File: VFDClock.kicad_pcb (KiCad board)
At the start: 2 copper layers, 76.2 x 53.3 mm, 22 parts, among them J1 Barrel_Jack_MountingPin, P1 Power, P2 Analog, P3 Digital, P4 Digital, Q1 VFD_LD8035E, Q2 VFD_LD8035E, Q3 VFD_LD8035E, Q4 VFD_LD8035E, Q5 VFD_LD8035E, Q6 VFD_LD8035E, U1 IC_HT16K33, U2 RTC_DS3231

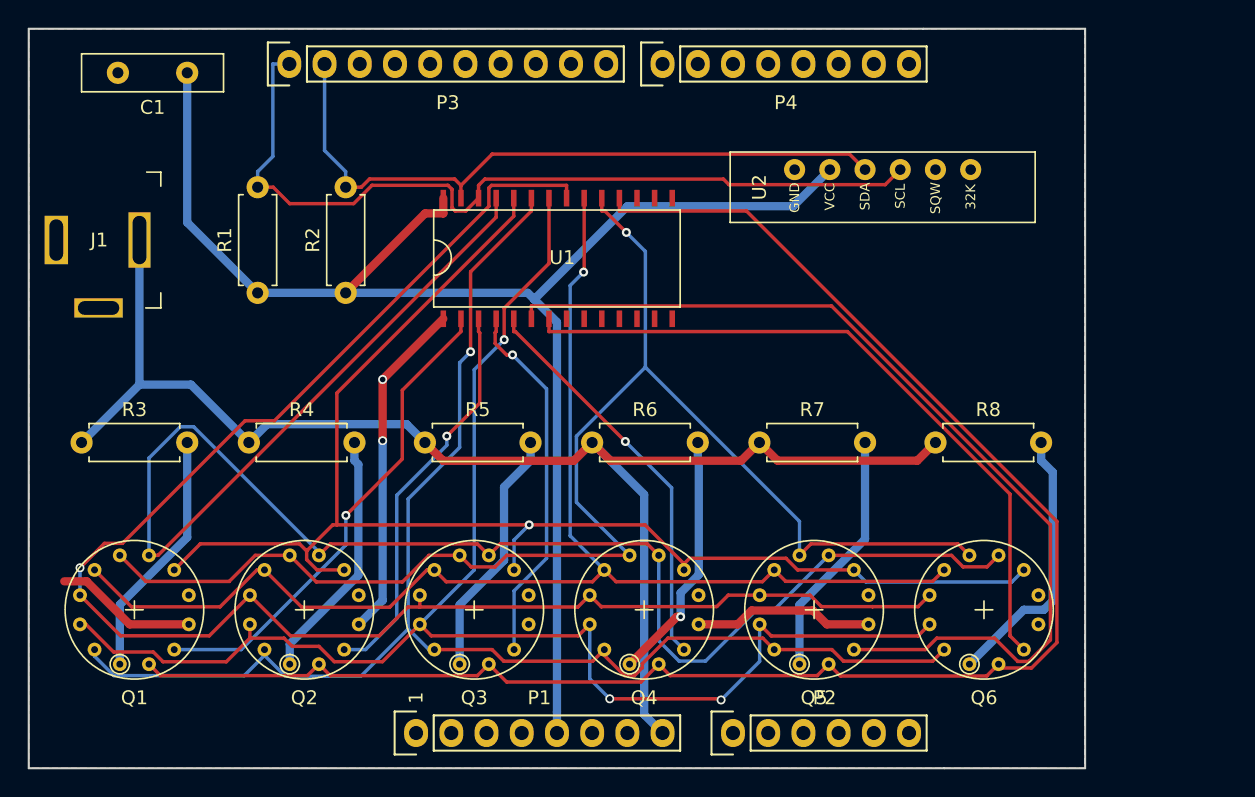
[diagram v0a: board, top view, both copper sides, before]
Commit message: 部品を仮配置
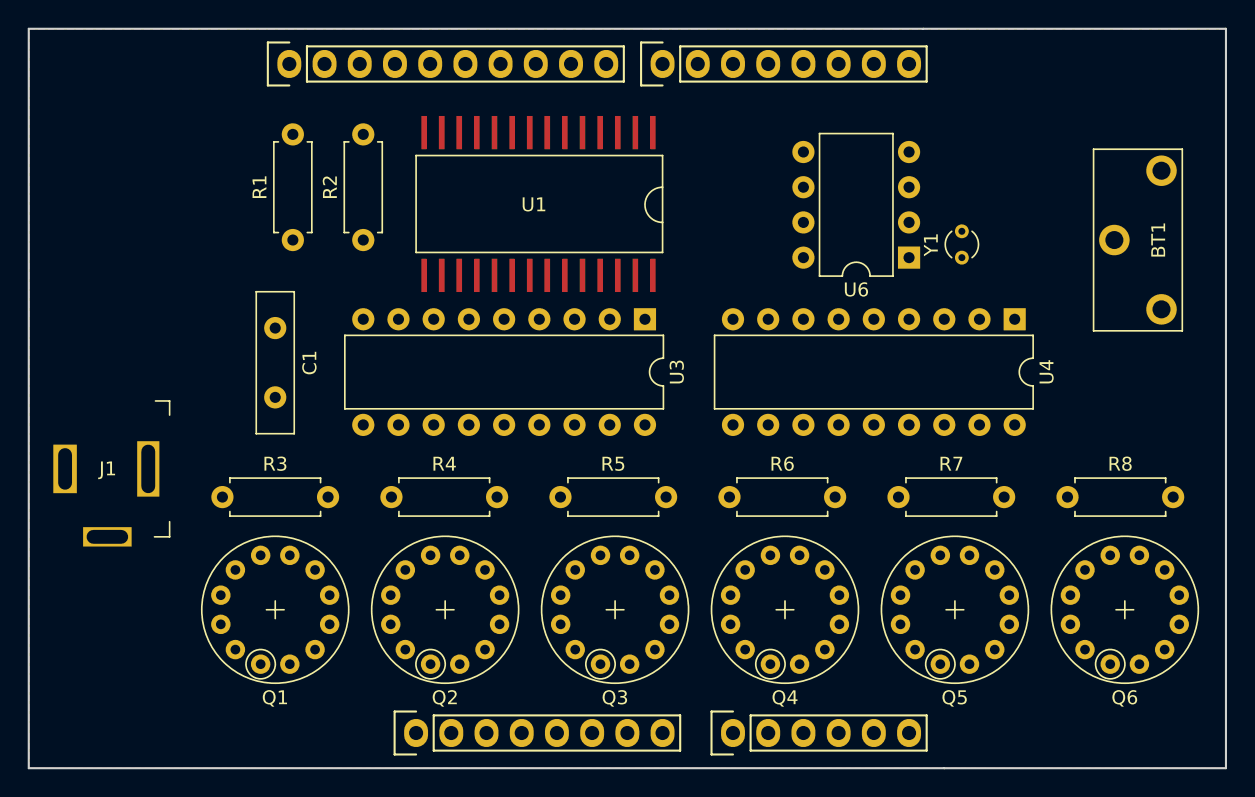
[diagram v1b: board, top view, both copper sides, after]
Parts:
- removed U2: RTC_DS3231, #MyFootPrints:RTC_DS3231_Vertical
- added BT1: Battery_Cell, #MyFootPrints:Battery_CR2032_CH74-2032LF, F.Cu at (191.0, 88.3)
- added U3: TBD62783APG, Package_DIP:DIP-18_W7.62mm, F.Cu at (155.4, 94.0)
- added U4: TBD62783APG, Package_DIP:DIP-18_W7.62mm, F.Cu at (182.1, 94.0)
- added U6: DS1307+, Package_DIP:DIP-8_W7.62mm, F.Cu at (174.5, 89.5)
- added Y1: 32.768kHz, Crystal:Crystal_DS26_D2.0mm_L6.0mm_Vertical, F.Cu at (178.3, 89.5)
- R3, R4, R5, R6, R7, R8: value 560 -> 510
- moved U1 20.1 mm to (156.7, 81.9), turned to 270 degrees
- moved C1 19.5 mm to (128.8, 94.6), turned to 270 degrees
- moved J1 16.5 mm to (105.9, 104.8)
- moved R4 11.0 mm to (137.2, 106.8)
- moved R3 10.9 mm to (125.0, 106.8)
- moved R7 10.8 mm to (173.7, 106.8)
- moved R6 10.7 mm to (161.5, 106.8)
- moved R5 10.5 mm to (149.4, 106.8)
- moved R8 10.3 mm to (185.9, 106.8)
- moved Q5 10.2 mm to (177.8, 114.9)
- moved Q1 10.2 mm to (128.8, 114.9)
- moved Q2 10.2 mm to (141.0, 114.9)
- moved Q3 10.2 mm to (153.3, 114.9)
- moved Q4 10.2 mm to (165.5, 114.9)
- moved Q6 10.2 mm to (190.1, 114.9)
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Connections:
- U1 pad 18: /dp -> Net-(U1-Pad18)
- U1 pad 19: /g -> Net-(U1-Pad19)
- U1 pad 2: Net-(Q1-Pad3) -> Net-(U1-Pad2)
- U1 pad 20: /f -> Net-(U1-Pad20)
- U1 pad 21: /e -> Net-(U1-Pad21)
- U1 pad 22: /d -> Net-(U1-Pad22)
- U1 pad 23: /c -> Net-(U1-Pad23)
- U1 pad 24: /b -> Net-(U1-Pad24)
- U1 pad 25: /a -> Net-(U1-Pad25)
- U1 pad 3: Net-(Q2-Pad3) -> Net-(U1-Pad3)
- U1 pad 4: Net-(Q3-Pad3) -> Net-(U1-Pad4)
- U1 pad 5: Net-(Q4-Pad3) -> Net-(U1-Pad5)
- U1 pad 6: Net-(Q5-Pad3) -> Net-(U1-Pad6)
- U1 pad 7: Net-(Q6-Pad3) -> Net-(U1-Pad7)
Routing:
- net /a: track 121.7 -> 0.00 mm
- net /dp: track 120.7 -> 0.00 mm
- net /e: track 118.6 -> 0.00 mm, vias 1 -> 0
- net /d: track 110.3 -> 0.00 mm, vias 3 -> 0
- net +5V: track 105.8 -> 0.00 mm
- net /c: track 104.7 -> 0.00 mm, vias 1 -> 0
- net +12V: track 102.9 -> 0.00 mm
- net /g: track 102.6 -> 0.00 mm, vias 1 -> 0
- net /b: track 102.1 -> 0.00 mm, vias 1 -> 0
- net /f: track 96.1 -> 0.00 mm, vias 1 -> 0
- net Net-(Q5-Pad3): track 69.1 -> 0.00 mm
- net /A5(SCL): track 61.6 -> 0.00 mm
- net Net-(Q6-Pad3): track 50.7 -> 0.00 mm
- net /A4(SDA): track 49.7 -> 0.00 mm
- net GND: track 47.9 -> 0.00 mm, vias 2 -> 0
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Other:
- board size 76.2 x 53.3 mm -> 86.4 x 53.3 mm
- board text removed: "1"

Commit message: 自動配線
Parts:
- moved U1 0.64 mm to (156.7, 81.3)
- turned BT1 to 270 degrees
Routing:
- net +12V: track 0.00 -> 150.4 mm
- net GND: track 0.00 -> 142.4 mm, vias 0 -> 1
- net /e: track 0.00 -> 112.1 mm, vias 0 -> 2
- net /dp: track 0.00 -> 107.5 mm, vias 0 -> 3
- net +5V: track 0.00 -> 101.0 mm, vias 0 -> 1
- net /b: track 0.00 -> 98.0 mm, vias 0 -> 1
- net /c: track 0.00 -> 96.2 mm
- net Net-(Q1-Pad3): track 0.00 -> 93.4 mm, vias 0 -> 1
- net /f: track 0.00 -> 92.2 mm, vias 0 -> 1
- net /a: track 0.00 -> 91.1 mm, vias 0 -> 2
- net /g: track 0.00 -> 88.7 mm
- net /d: track 0.00 -> 83.6 mm, vias 0 -> 1
- net /A5(SCL): track 0.00 -> 71.9 mm
- net /A4(SDA): track 0.00 -> 54.4 mm
- net Net-(Q2-Pad1): track 0.00 -> 47.1 mm, vias 0 -> 1
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
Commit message: ベタ修正
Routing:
- net GND: track 142.4 -> 108.1 mm
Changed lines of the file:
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@@
     (thickness 1.6)
     (drawings 14)
-    (tracks 569)
+    (tracks 565)
     (zones 0)
     (modules 26)
@@
     (trace_clearance 0.2)
     (zone_clearance 0.508)
-    (zone_45_only no)
+    (zone_45_only yes)
     (trace_min 0.2)
     (via_size 0.65)
@@
   (segment (start 186.395 120.65) (end 186.563 120.65) (width 0.6) (layer B.Cu) (net 2))
   (segment (start 181.732 115.987) (end 186.395 120.65) (width 0.6) (layer B.Cu) (net 2))
-  (segment (start 128.778 99.615) (end 118.778 99.615) (width 0.6) (layer B.Cu) (net 2))
-  (segment (start 118.778 99.615) (end 113.618 104.775) (width 0.6) (layer B.Cu) (net 2))
   (segment (start 135.128 101.6) (end 130.763 101.6) (width 0.6) (layer B.Cu) (net 2))
   (segment (start 130.763 101.6) (end 128.778 99.615) (width 0.6) (layer B.Cu) (net 2))
@@
   (segment (start 137.367 120.65) (end 148.463 120.65) (width 0.6) (layer B.Cu) (net 2))
   (segment (start 148.463 120.65) (end 151.638 123.825) (width 0.6) (layer B.Cu) (net 2))
-  (segment (start 156.023 79.88) (end 161.798 79.88) (width 0.6) (layer F.Cu) (net 2))
-  (segment (start 161.798 79.88) (end 161.798 79.88) (width 0.6) (layer F.Cu) (net 2))
-  (via (at 161.798 79.88) (size 0.65) (drill 0.4) (layers F.Cu B.Cu) (net 2))
   (segment (start 174.498 81.207876) (end 174.498 81.915) (width 0.6) (layer B.Cu) (net 2))
-  (segment (start 173.170124 79.88) (end 174.498 81.207876) (width 0.6) (layer B.Cu) (net 2))
-  (segment (start 161.798 79.88) (end 173.170124 79.88) (width 0.6) (layer B.Cu) (net 2))
+  (segment (start 156.023 79.88) (end 157.988 79.88) (width 0.6) (layer F.Cu) (net 2))
+  (segment (start 157.988 79.88) (end 157.988 79.88) (width 0.6) (layer F.Cu) (net 2))
+  (via (at 157.988 79.88) (size 0.65) (drill 0.4) (layers F.Cu B.Cu) (net 2))
   (segment (start 147.6584 81.4186) (end 147.6584 78.7605) (width 0.25) (layer F.Cu) (net 3))
   (segment (start 147.6584 78.7605) (end 148.0643 78.3546) (width 0.25) (layer F.Cu) (net 3))
@@
       )
     )
+  )
+  (zone (net 0) (net_name "") (layers F&B.Cu) (hatch edge 0.508)
+    (connect_pads (clearance 0.508))
+    (min_thickness 0.254)
+    (keepout (tracks allowed) (vias allowed) (copperpour not_allowed))
+    (fill (arc_segments 32) (thermal_gap 0.508) (thermal_bridge_width 0.508))
+    (polygon
+      (pts
+        (xy 195.453 117.475) (xy 192.278 120.65) (xy 126.238 120.65) (xy 124.333 118.745) (xy 124.333 112.395)
+        (xy 126.873 109.855) (xy 195.453 109.855)
+      )
+    )
+  )
+  (zone (net 0) (net_name "") (layer F.Cu) (hatch edge 0.508)
+    (connect_pads (clearance 0.508))
+    (min_thickness 0.254)
+    (keepout (tracks allowed) (vias allowed) (copperpour not_allowed))
+    (fill (arc_segments 32) (thermal_gap 0.508) (thermal_bridge_width 0.508))
+    (polygon
+      (pts
+        (xy 166.243 82.55) (xy 166.243 90.805) (xy 165.608 90.805) (xy 156.083 81.28) (xy 156.083 78.74)
+        (xy 162.433 78.74)
+      )
+    )
+  )
+  (zone (net 0) (net_name "") (layer F.Cu) (hatch edge 0.508)
+    (connect_pads (clearance 0.508))
+    (min_thickness 0.254)
+    (keepout (tracks allowed) (vias allowed) (copperpour not_allowed))
+    (fill (arc_segments 32) (thermal_gap 0.508) (thermal_bridge_width 0.508))
+    (polygon
+      (pts
+        (xy 161.798 106.045) (xy 160.528 106.045) (xy 160.528 102.235) (xy 164.338 102.235)
+      )
+    )
+  )
+  (zone (net 0) (net_name "") (layer F.Cu) (hatch edge 0.508)
+    (connect_pads (clearance 0.508))
+    (min_thickness 0.254)
+    (keepout (tracks allowed) (vias allowed) (copperpour not_allowed))
+    (fill (arc_segments 32) (thermal_gap 0.508) (thermal_bridge_width 0.508))
+    (polygon
+      (pts
+        (xy 161.163 92.71) (xy 161.163 94.615) (xy 159.258 96.52) (xy 159.258 104.775) (xy 156.083 104.775)
+        (xy 154.813 106.045) (xy 150.368 106.045) (xy 147.828 107.315) (xy 131.318 107.315) (xy 131.318 99.695)
+        (xy 135.763 94.615) (xy 156.718 94.615) (xy 156.718 92.71) (xy 154.813 92.71) (xy 154.178 91.44)
+        (xy 156.718 91.44) (xy 156.718 89.535)
+      )
+    )

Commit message: 手で最適化
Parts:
- moved U1 1.42 mm to (156.1, 82.5)
- moved U3 1.02 mm to (155.4, 95.0)
- moved U4 1.02 mm to (182.1, 95.0)
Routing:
- net Net-(U1-Pad7): track 27.9 -> 71.2 mm, vias 1 -> 0
- net Net-(Q2-Pad3): track 44.7 -> 83.2 mm
- net Net-(U1-Pad6): track 30.7 -> 65.8 mm
- net Net-(U1-Pad5): track 29.9 -> 60.2 mm
- net Net-(U1-Pad4): track 31.2 -> 54.5 mm
- net /e: track 112.1 -> 91.0 mm, vias 2 -> 3
- net Net-(U1-Pad3): track 32.5 -> 49.0 mm
- net /A5(SCL): track 71.9 -> 60.3 mm, vias 0 -> 1
- net GND: track 108.1 -> 115.9 mm, vias 1 -> 0
- net Net-(U1-Pad2): track 33.7 -> 41.2 mm
- net Net-(Q5-Pad3): track 29.9 -> 34.1 mm
- net +5V: track 101.0 -> 105.0 mm
- net +12V: track 150.4 -> 147.8 mm
- net /b: track 98.0 -> 100.5 mm
- net Net-(Q1-Pad3): track 93.4 -> 95.1 mm
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
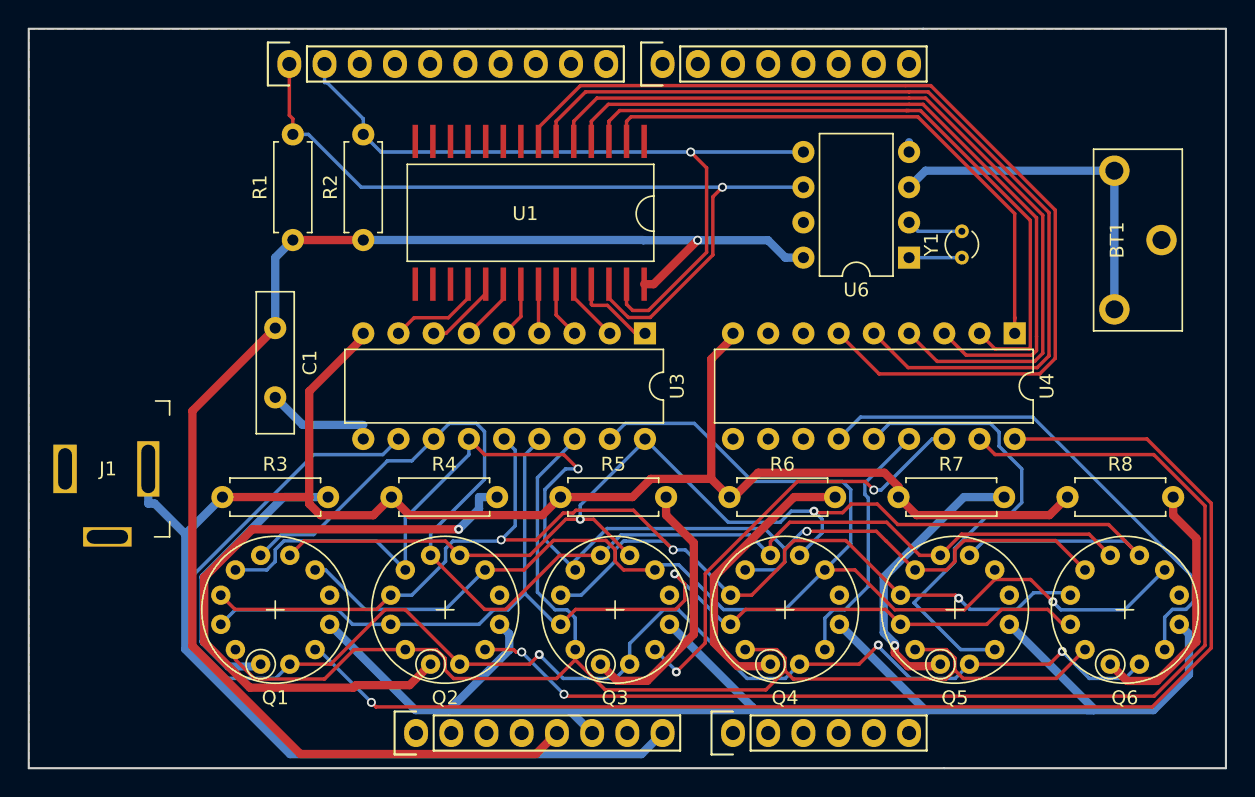
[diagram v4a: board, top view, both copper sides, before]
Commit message: ベタ形状を修正
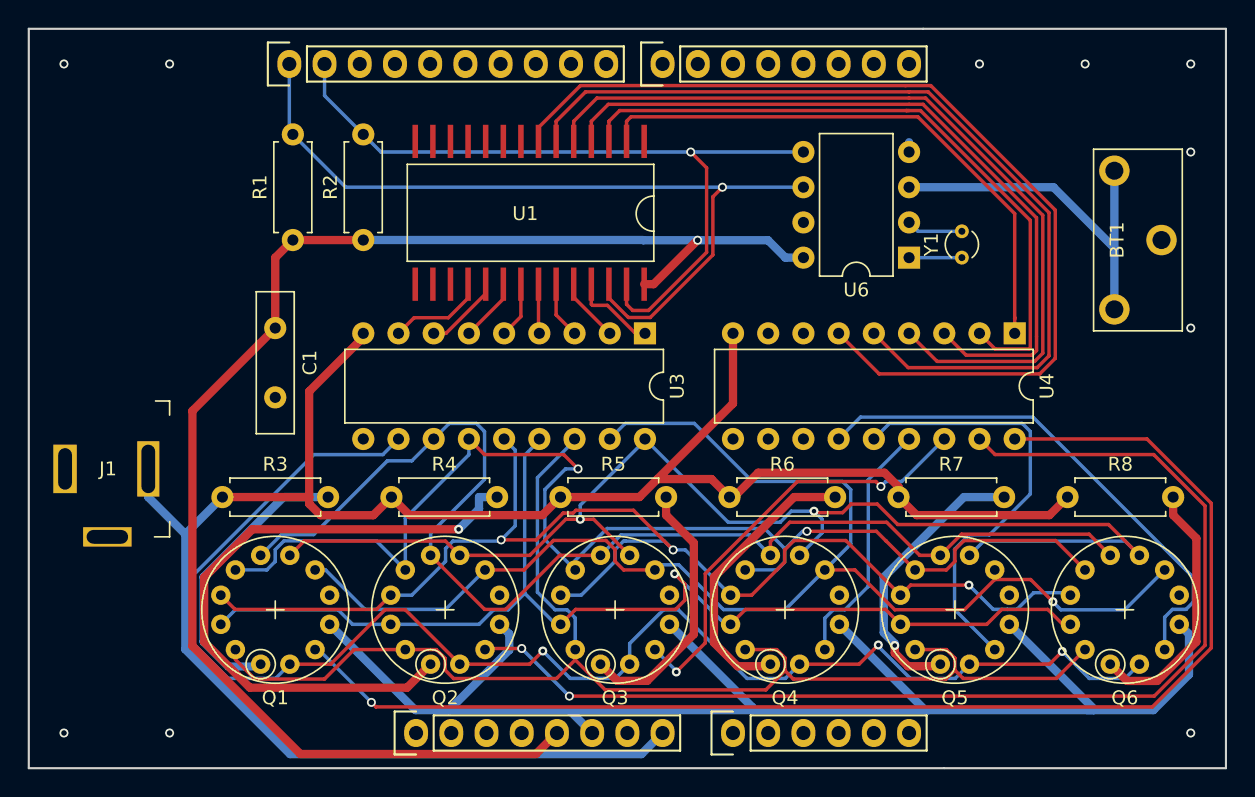
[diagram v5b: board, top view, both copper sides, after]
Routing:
- net GND: track 115.9 -> 108.7 mm, vias 0 -> 10
- net Net-(Q5-Pad3): track 34.1 -> 32.1 mm
- net +12V: track 147.8 -> 149.5 mm
- net +BATT: track 25.7 -> 27.1 mm
- net /e: track 91.0 -> 91.6 mm

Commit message: ロゴなどを追加
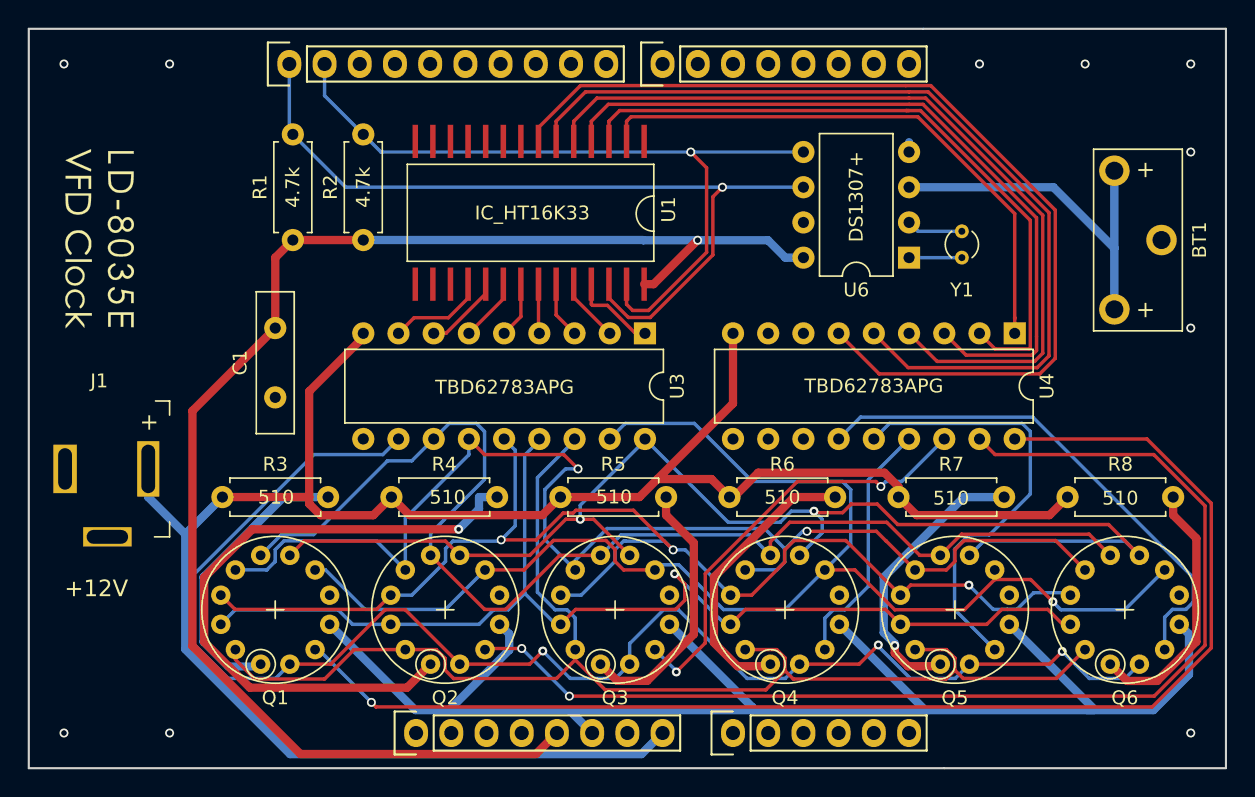
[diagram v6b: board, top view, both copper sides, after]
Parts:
- added G***: LOGO, logo:logo, F.Cu at (116.1, 88.2)
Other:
- board text added: "+"
- board text added: "+12V"
